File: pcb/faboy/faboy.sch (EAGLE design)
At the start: 0 parts

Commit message: schematics oled and cpu
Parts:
- added C1, C2, C5, C6, C7: 1uF, resistor:C-EUC0805K
- added C3: 4.7uF / 10v, resistor:C-EUC0805K
- added C4: 2.2uF, resistor:C-EUC0805K
- added CN1: (no value), adafruit:USBMINIB
- added F1: (no value), adafruit:PTCFUSE-1812
- added R1: 390k, resistor:R-EU_R0805
- added R2: 10k, resistor:R-EU_R0805
- added R3, R4: 22, resistor:R-EU_R0805
- added U$1: UG-2864HSWEG01, adafruit:UG-2864HSWEG01
- added U$2: ATMEGA32U4-AU, adafruit:ATMEGA32U4-AU
- added Y1: 16MHZ, SparkFun-FreqCtrl:RESONATOR16MHZ
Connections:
- new net CLK: U$1.D0/DI
- new net CS: U$1./CS
- new net D+: R3.1, U$2.D+
- new net D-: R4.1, U$2.D-
- new net DC: U$1.D/C
- new net GND: C3.2, C4.2, C7.1, CN1.GND, R1.1, U$1.BS0, U$1.BS1, U$1.BS2, U$1.MT, U$1.MT2, U$1.VLSS, U$1.VSS, U$2.GND, U$2.GND1, U$2.GND2, U$2.GND3, Y1.2
- new net MOSI: U$1.D1/SCLK
- new net N$1: C1.1, U$1.C2P
- new net N$11: U$2.XTAL1, Y1.1
- new net N$12: CN1.D+, R3.2
- new net N$13: CN1.D-, R4.2
- new net N$14: U$2.XTAL2, Y1.3
- new net N$2: C1.2, U$1.C2N
- new net N$3: C2.1, U$1.C1P
- new net N$4: C2.2, U$1.C1N
- new net N$5: R1.2, U$1.IREF
- new net N$6: R2.1, U$2./RESET
- new net N$7: C3.1, U$1.VCOMH
- new net N$8: C4.1, U$1.VCC
- new net N$9: C7.2, U$2.UCAP
- new net OLED_RST: U$1./RES
- new net UVCC: CN1.VBUS, U$2.UVCC, U$2.VBUS
- new net VCC: R2.2, U$1.VBAT, U$1.VDD, U$2.AVCC, U$2.AVCC1, U$2.VCC, U$2.VCC1

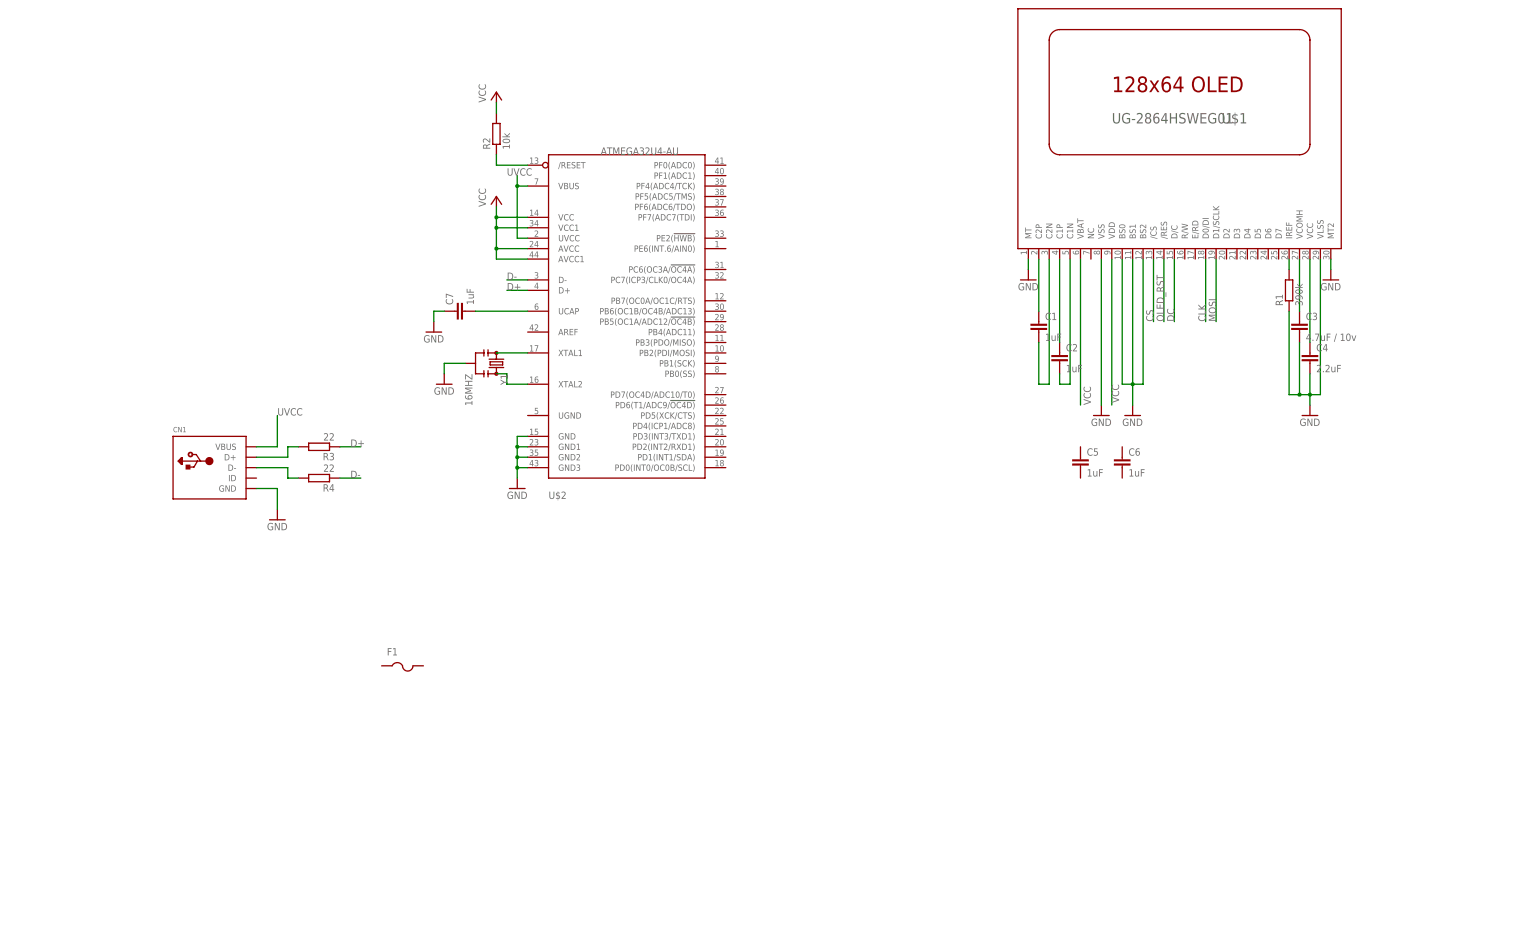
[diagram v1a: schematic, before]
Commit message: schematics leds on switch / pcb border
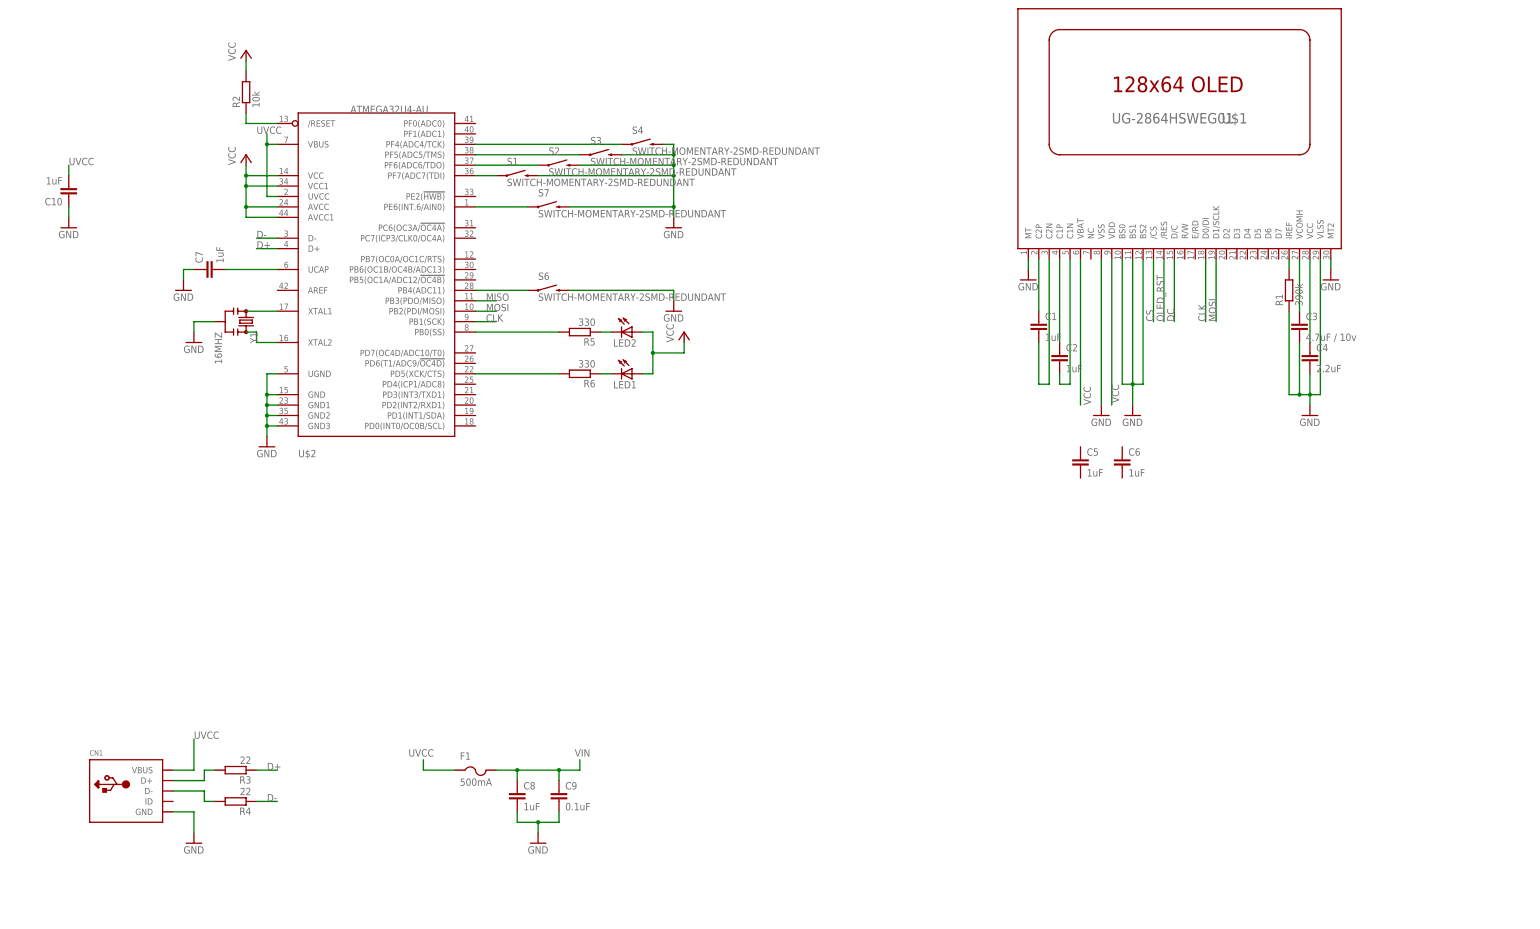
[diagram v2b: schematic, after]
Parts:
- added C10, C8: 1uF, resistor:C-EUC0805K
- added C9: 0.1uF, resistor:C-EUC0805K
- added LED1, LED2: (no value), led:LEDSML0805
- added R5, R6: 330, resistor:R-EU_R0805
- added S1, S2, S3, S4, S6, S7: SWITCH-MOMENTARY-2SMD-REDUNDANT, SparkFun-Electromechanical:SWITCH-MOMENTARY-2SMD-REDUNDANT
- F1: value (none) -> 500mA
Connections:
- new net MISO: U$2.PB3(PDO/MISO)
- new net N$10: S1.1, U$2.PF7(ADC7(TDI)
- new net N$15: S2.1, U$2.PF6(ADC6/TDO)
- new net N$16: S3.1, U$2.PF5(ADC5/TMS)
- new net N$17: S4.1, U$2.PF4(ADC4/TCK)
- new net N$18: S7.1, U$2.PE6(INT.6/AIN0)
- new net N$19: S6.1, U$2.PB4(ADC11)
- new net N$22: R5.2, U$2.PB0(SS)
- new net N$23: LED2.C, R5.1
- new net N$24: R6.2, U$2.PD5(XCK/CTS)
- new net N$25: LED1.C, R6.1
- new net VIN: C8.1, C9.1, F1.2
- net CLK: now also U$2.PB1(SCK)
- net GND: now also C10.1, C8.2, C9.2, S1.2, S2.2, S3.2, S4.2, S6.2, S7.2, U$2.UGND
- net MOSI: now also U$2.PB2(PDI/MOSI)
- net UVCC: now also C10.2, F1.1
- net VCC: now also LED1.A, LED2.A
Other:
- moved on the sheet: C7, CN1, F1, R2, R3, R4, U$2, Y1

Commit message: schematics > dcdc, switch and battery / pcb > round courner
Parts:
- added BAT1: (no value), SparkFun-Electromechanical:BATTERY20SMD
- added C11, C12, C13: 1uF, resistor:C-EUC0805K
- added S5: (no value), SparkFun-Electromechanical:SWITCH-SPDT-SMD-A
- added S8: SWITCH-MOMENTARY-2SMD-3, SparkFun-Electromechanical:SWITCH-MOMENTARY-2SMD-3
- added SG1: BUZZERSMD3, SparkFun-Electromechanical:BUZZERSMD3
- added U1: MAX1595UMAX, maxim:MAX1595UMAX
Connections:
- net N$10 renamed DOWN
- net N$15 renamed LEFT
- net N$16 renamed RIGHT
- net N$17 renamed UP
- net N$18 renamed A
- net N$19 renamed B
- new net N$10: C12.1, S5.O, U1.!SHDN, U1.IN
- new net N$15: C11.1, U1.CXN
- new net N$16: C11.2, U1.CXP
- net GND: now also C12.2, C13.2, C5.2, C6.2, S8.1, U1.GND, U1.PGND
- net N$6: now also S8.2
- net VCC: now also C13.1, C5.1, C6.1, U1.AOUT, U1.OUT
- net VIN: now also BAT1.+, S5.P
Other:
- moved on the sheet: C5, C6, S1, S2, S3, S4, S7

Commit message: schematics > rgb led / pcb > via size route
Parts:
- added C14, C15, C16: 4.7uF, resistor:C-EUC0805K
- added J1: (no value), SparkFun-Connectors:M03X2
- added J2: (no value), SparkFun-Connectors:M06SMD-FEMALE-V2
- added LED3: (no value), led:LEDSML0805
- added LED6: GM5WA94310A, led:GM5WA94310A
- added R10, R11, R9: 330, resistor:R-EU_R0805
- added R7: 390k, resistor:R-EU_R0805
- added R8: 470, resistor:R-EU_R0805
- added SJ1: (no value), jumper:SJ
- added SJ2: (no value), jumper:SJ2W
- added U2: MCP73831, SparkFun-PowerIC:MCP73831
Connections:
- removed net CLK: U$1.D0/DI, U$2.PB1(SCK)
- new net N$17: R8.1, U2.STAT
- new net N$18: LED3.C, R8.2
- new net N$19: R7.2, U2.PROG
- new net N$20: C16.2, U$2.PC6(OC3A/!OC4A)
- new net N$21: C16.1, SG1.1
- new net N$26: SG1.2, SJ2.2
- new net N$27: SJ2.3, U$2.PC7(ICP3/CLK0/OC4A)
- new net N$28: R10.2, U$2.PB6(OC1B/OC4B/ADC13)
- new net N$29: R11.2, U$2.PB7(OC0A/OC1C/RTS)
- new net N$30: LED6R.C, R11.1
- new net N$31: LED6G.C, R10.1
- new net N$32: LED6B.C, R9.1
- new net RST: J2.2, R2.1, S8.2, U$2./RESET
- new net SCLK: J2.3, U$1.D0/DI, U$2.PB1(SCK)
- new net VBAT: BAT1.+, C15.1, U2.VBAT
- net CS: now also U$2.PD6(T1/ADC9/!OC4D)
- net DC: now also U$2.PD4(ICP1/ADC8)
- net GND: now also BAT1.-, C14.2, C15.2, J2.1, R7.1, SJ2.1, U2.VSS
- net MISO: now also J2.4
- net MOSI: now also J2.5
- net N$10: now also SJ1.1
- net N$6: now also R9.2, U$2.PB5(OC1A/ADC12/!OC4B); no longer R2.1, S8.2, U$2./RESET
- net OLED_RST: now also U$2.PD7(OC4D/ADC10/T0)
- net VCC: now also J2.6, LED6B.A, LED6G.A, LED6R.A, SJ1.2
- net VIN: now also C14.1, LED3.A, U2.VIN; no longer BAT1.+, S5.P
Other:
- note added: "direct power"
- moved on the sheet: BAT1, C11, C12, C13, C8, C9, CN1, F1, LED1, LED2, R3, R4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

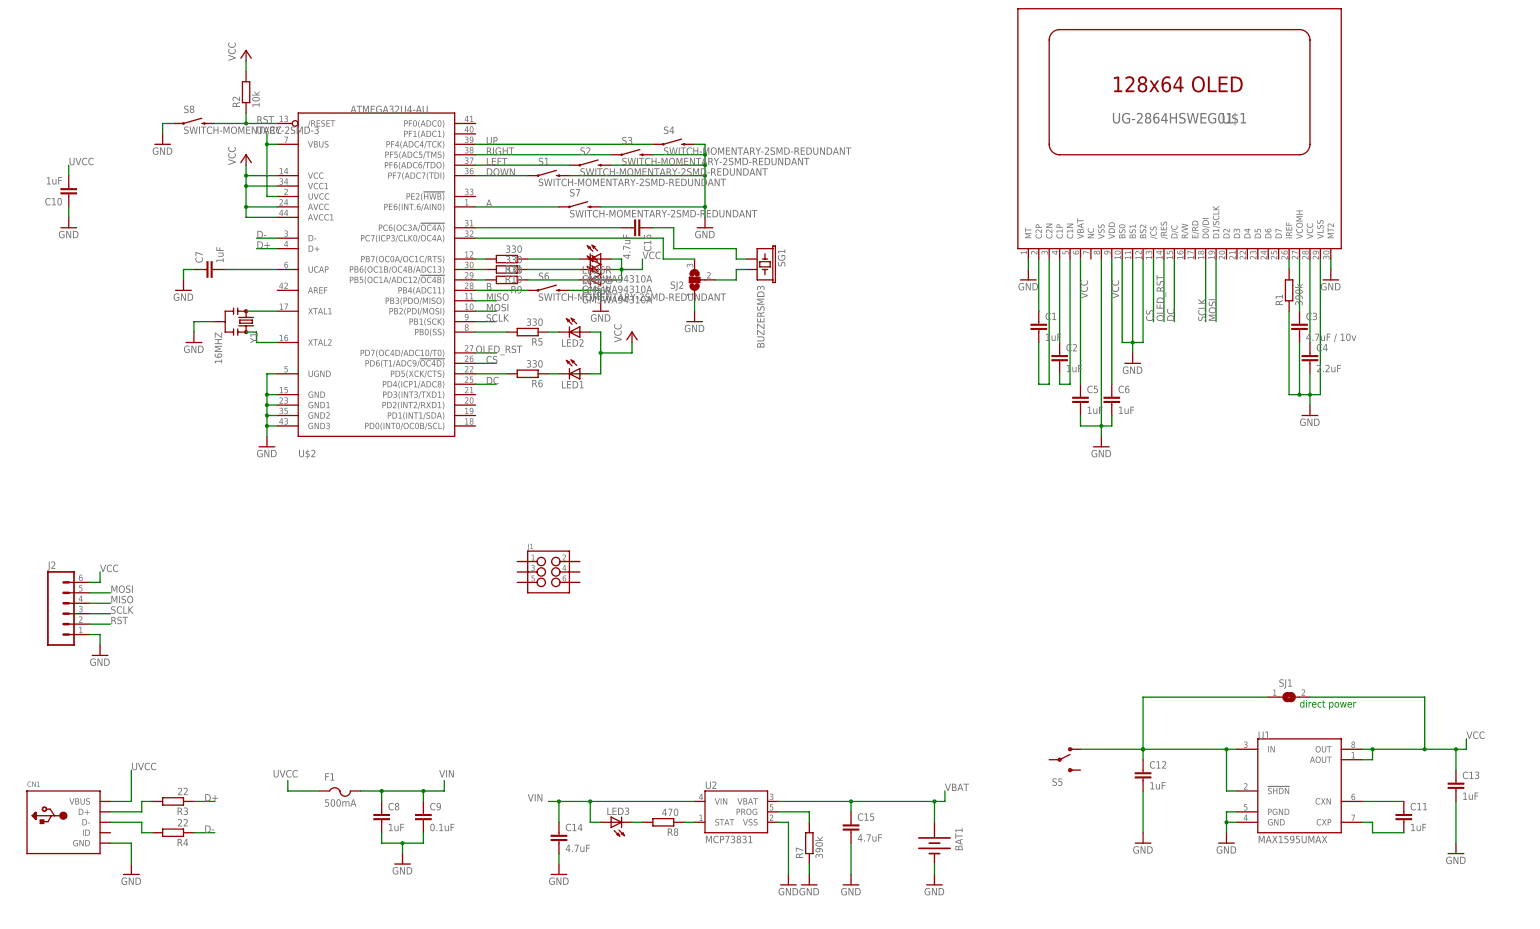
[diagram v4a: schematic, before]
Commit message: pcb > start to re-arange the pin
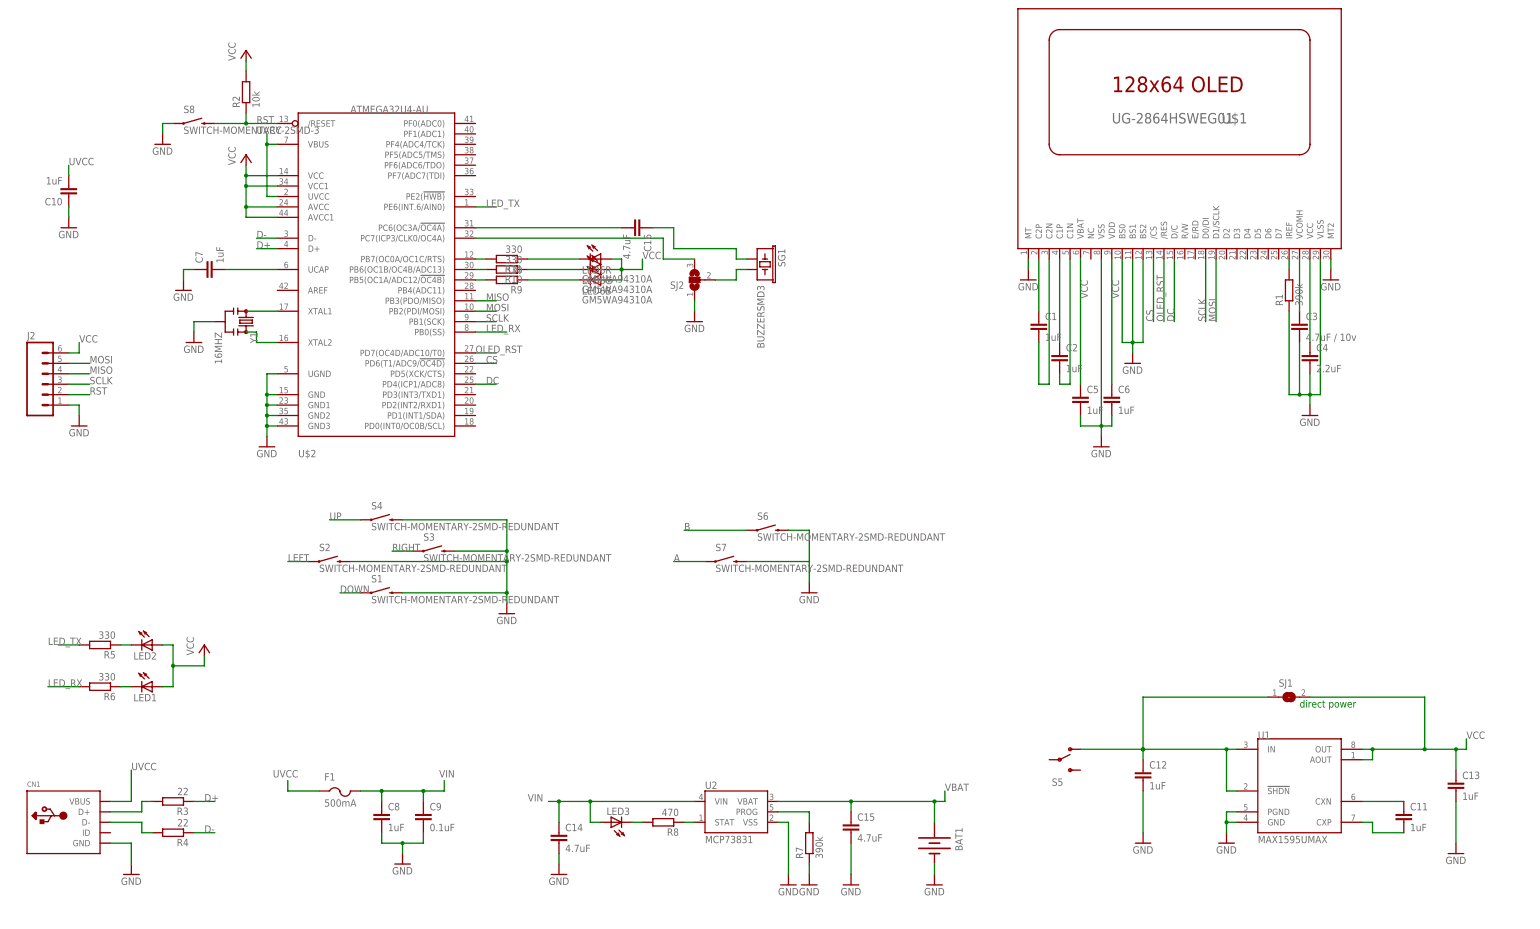
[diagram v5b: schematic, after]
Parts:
- removed J1: (no value), SparkFun-Connectors:M03X2
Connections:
- removed net N$22: R5.2, U$2.PB0(SS)
- removed net N$24: R6.2, U$2.PD5(XCK/CTS)
- new net LED_RX: R6.2, U$2.PB0(SS)
- new net LED_TX: R5.2, U$2.PE6(INT.6/AIN0)
- net A: no longer U$2.PE6(INT.6/AIN0)
- net B: no longer U$2.PB4(ADC11)
- net DOWN: no longer U$2.PF7(ADC7(TDI)
- net LEFT: no longer U$2.PF6(ADC6/TDO)
- net RIGHT: no longer U$2.PF5(ADC5/TMS)
- net UP: no longer U$2.PF4(ADC4/TCK)
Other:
- moved on the sheet: J2, LED1, LED2, R5, R6, S1, S2, S3, S4, S6, S7

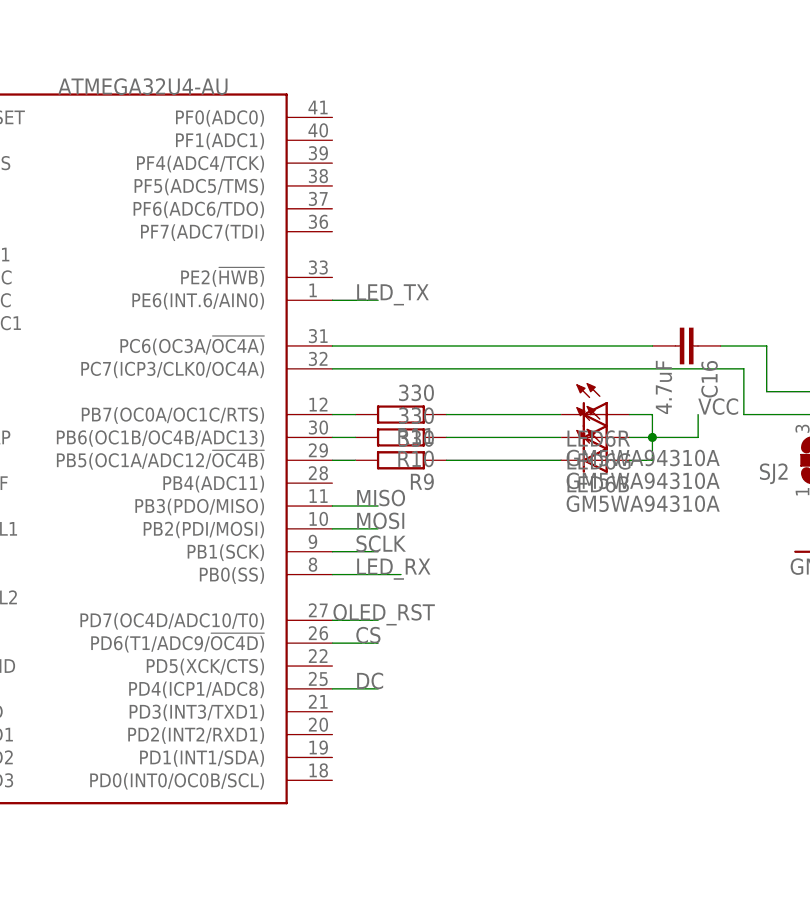
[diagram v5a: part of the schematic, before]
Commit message: pcb > route oled, a and b pushbutton / change via size to 0.4mm / add QR code on layer 200 and 2001
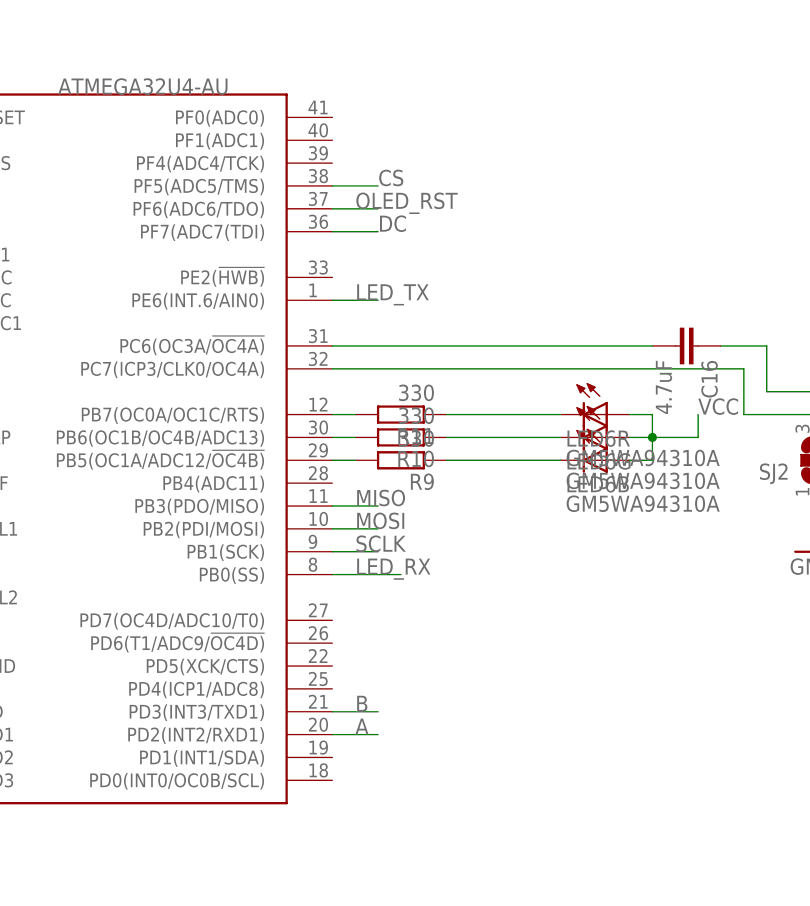
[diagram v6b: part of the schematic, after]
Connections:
- net A: now also U$2.PD2(INT2/RXD1)
- net B: now also U$2.PD3(INT3/TXD1)
- net CS: now also U$2.PF5(ADC5/TMS); no longer U$2.PD6(T1/ADC9/!OC4D)
- net DC: now also U$2.PF7(ADC7(TDI); no longer U$2.PD4(ICP1/ADC8)
- net OLED_RST: now also U$2.PF6(ADC6/TDO); no longer U$2.PD7(OC4D/ADC10/T0)
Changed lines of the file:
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@@
 </segment>
 <segment>
-<pinref part="U$2" gate="G$1" pin="PD6(T1/ADC9/!OC4D)"/>
-<wire x1="121.92" y1="152.4" x2="127" y2="152.4" width="0.1524" layer="91"/>
-<label x="124.46" y="152.4" size="1.778" layer="95"/>
+<pinref part="U$2" gate="G$1" pin="PF5(ADC5/TMS)"/>
+<wire x1="121.92" y1="203.2" x2="127" y2="203.2" width="0.1524" layer="91"/>
+<label x="127" y="203.2" size="1.778" layer="95"/>
 </segment>
 </net>
@@
 </segment>
 <segment>
-<pinref part="U$2" gate="G$1" pin="PD7(OC4D/ADC10/T0)"/>
-<wire x1="121.92" y1="154.94" x2="127" y2="154.94" width="0.1524" layer="91"/>
-<label x="121.92" y="154.94" size="1.778" layer="95"/>
+<pinref part="U$2" gate="G$1" pin="PF6(ADC6/TDO)"/>
+<wire x1="121.92" y1="200.66" x2="127" y2="200.66" width="0.1524" layer="91"/>
+<label x="124.46" y="200.66" size="1.778" layer="95"/>
 </segment>
 </net>
@@
 </segment>
 <segment>
-<pinref part="U$2" gate="G$1" pin="PD4(ICP1/ADC8)"/>
-<wire x1="121.92" y1="147.32" x2="127" y2="147.32" width="0.1524" layer="91"/>
-<label x="124.46" y="147.32" size="1.778" layer="95"/>
+<pinref part="U$2" gate="G$1" pin="PF7(ADC7(TDI)"/>
+<wire x1="121.92" y1="198.12" x2="127" y2="198.12" width="0.1524" layer="91"/>
+<label x="127" y="198.12" size="1.778" layer="95"/>
 </segment>
 </net>
@@
 <label x="172.72" y="111.76" size="1.778" layer="95"/>
 </segment>
+<segment>
+<pinref part="U$2" gate="G$1" pin="PD3(INT3/TXD1)"/>
+<wire x1="121.92" y1="144.78" x2="127" y2="144.78" width="0.1524" layer="91"/>
+<label x="124.46" y="144.78" size="1.778" layer="95"/>
+</segment>
 </net>
 <net name="A" class="0">
@@
 <label x="170.18" y="104.14" size="1.778" layer="95"/>
 </segment>
-</net>
+<segment>
+<pinref part="U$2" gate="G$1" pin="PD2(INT2/RXD1)"/>
+<wire x1="121.92" y1="142.24" x2="127" y2="142.24" width="0.1524" layer="91"/>
+<label x="124.46" y="142.24" size="1.778" layer="95"/>
+</segment>
+</net>
